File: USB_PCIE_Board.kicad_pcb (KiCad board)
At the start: 4 copper layers, 98.2 x 111.5 mm, 171 parts, among them J1 Bus_PCI_Express_x1, J2 0484050001, J3 0484050001, J4 0484050001, J5 0484050001, Q1 2SA1576AT106R, Q2 2SC4081T106R, Q4 DMT6016LSS-13, Q5 SI4134DY-T1-GE3, U1 UPD720201K8-711-BAC-A, U10 AP2191SG-13, U11 AP2191SG-13, U12 SP3011-06UTG, U13 SP3011-06UTG, U14 SP3011-06UTG, U15 SP3011-06UTG, U2 MX25L4006EM1I-12G, U3 LM22678TJ-5.0/NOPB, U4 LTC3872ETS8-TRPBF, U5 RT5762CHGH6F, U6 641737-1, U7 AP7215-33YG-13, U8 AP2191SG-13, U9 AP2191SG-13, X1 CS14522-24M

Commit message: Fix some DRC no-connect issues
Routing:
- net GND: track 86.0 -> 98.7 mm, vias 164 -> 167
- added copper zone on In2.Cu, net GND
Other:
- outline, holes or cut-outs redrawn
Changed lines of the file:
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@@
 		(layer "Edge.Cuts")
 	)
+	(gr_circle
+		(center 90.236099 106.301955)
+		(end 91.05 106.301955)
+		(stroke
+			(width 0.2)
+			(type default)
+		)
+		(fill no)
+		(layer "Edge.Cuts")
+	)
 	(gr_line
 		(start 92.79875 138.837708)
@@
 	)
 	(via
-		(at 93.9 100.8)
+		(at 93.82 100.28)
 		(size 0.35)
 		(drill 0.2)
@@
 	)
 	(via
+		(at 91.475 106.275)
+		(size 1)
+		(drill 0.4)
+		(layers "F.Cu" "B.Cu")
+		(net "GND")
+	)
+	(via
 		(at 86.4 101.2)
 		(size 0.35)
@@
 	)
 	(via
+		(at 90.225 107.525)
+		(size 1)
+		(drill 0.4)
+		(layers "F.Cu" "B.Cu")
+		(net "GND")
+	)
+	(via
 		(at 111.15 63.3)
 		(size 1)
@@
 	)
 	(via
+		(at 89 106.3)
+		(size 1)
+		(drill 0.4)
+		(layers "F.Cu" "B.Cu")
+		(net "GND")
+	)
+	(via
 		(at 124.303098 93.143309)
 		(size 0.35)
@@
 	)
 	(via
-		(at 90.2249 106.299999)
-		(size 1)
-		(drill 0.4)
+		(at 90.212351 112.228286)
+		(size 0.35)
+		(drill 0.2)
 		(layers "F.Cu" "B.Cu")
 		(net "GND")
 	)
 	(via
-		(at 90.212351 112.228286)
-		(size 0.35)
-		(drill 0.2)
+		(at 90.25 105)
+		(size 1)
+		(drill 0.4)
 		(layers "F.Cu" "B.Cu")
 		(net "GND")
@@
 	)
 	(segment
+		(start 113.6 142.3)
+		(end 113.5 142.3)
+		(width 0.5)
+		(layer "B.Cu")
+		(net "GND")
+	)
+	(segment
 		(start 84.3 102.7)
 		(end 84.3025 102.7)
@@
 	)
 	(segment
+		(start 115.7 142.3)
+		(end 115.999588 142.599588)
+		(width 0.5)
+		(layer "B.Cu")
+		(net "GND")
+	)
+	(segment
+		(start 93.81 100.29)
+		(end 93.81 100.36)
+		(width 0.2)
+		(layer "B.Cu")
+		(net "GND")
+	)
+	(segment
 		(start 93.13 112.17)
 		(end 93.13 111.53)
@@
 	)
 	(segment
+		(start 93.4225 100.7475)
+		(end 93.4225 100.8)
+		(width 0.2)
+		(layer "B.Cu")
+		(net "GND")
+	)
+	(segment
 		(start 86.4 101.2)
 		(end 87.0425 101.2)
@@
 	)
 	(segment
-		(start 93.9 100.8)
-		(end 93.4225 100.8)
-		(width 0.2)
-		(layer "B.Cu")
-		(net "GND")
-	)
-	(segment
 		(start 92.633072 100.286055)
 		(end 92.413945 100.286055)
@@
 	)
 	(segment
+		(start 113.1 142.7)
+		(end 113.1 146.3)
+		(width 0.5)
+		(layer "B.Cu")
+		(net "GND")
+	)
+	(segment
 		(start 84.9 110.2)
 		(end 84.9 109.4825)
@@
 	)
 	(segment
+		(start 115.999588 142.599588)
+		(end 115.999588 146.3)
+		(width 0.5)
+		(layer "B.Cu")
+		(net "GND")
+	)
+	(segment
 		(start 84.9 109.4825)
 		(end 85.0125 109.37)
@@
 	)
 	(segment
+		(start 113.5 142.3)
+		(end 113.1 142.7)
+		(width 0.5)
+		(layer "B.Cu")
+		(net "GND")
+	)
+	(segment
 		(start 84.39 105.39)
 		(end 84.995 105.39)
@@
 	)
 	(segment
+		(start 93.82 100.28)
+		(end 93.81 100.29)
+		(width 0.2)
+		(layer "B.Cu")
+		(net "GND")
+	)
+	(segment
 		(start 84.3 105.1)
 		(end 84.3 105.3)
@@
 	)
 	(segment
+		(start 110.148639 142.451361)
+		(end 110.148639 146.3)
+		(width 0.2)
+		(layer "B.Cu")
+		(net "GND")
+	)
+	(segment
 		(start 87.778884 112.232802)
 		(end 87.778884 111.946116)
@@
 	)
 	(segment
+		(start 110.3 142.3)
+		(end 110.148639 142.451361)
+		(width 0.2)
+		(layer "B.Cu")
+		(net "GND")
+	)
+	(segment
 		(start 91.418327 100.281673)
 		(end 91.13 100.57)
@@
 	)
 	(segment
+		(start 93.81 100.36)
+		(end 93.4225 100.7475)
+		(width 0.2)
+		(layer "B.Cu")
+		(net "GND")
+	)
+	(segment
 		(start 91.13 100.57)
 		(end 91.13 101.0925)
@@
 	)
 	(segment
-		(start 84.6 114.3)
-		(end 84.85 114.05)
+		(start 98 135.5)
+		(end 92.7 130.2)
 		(width 0.2)
 		(layer "F.Cu")
@@
 	)
 	(segment
-		(start 98 135.5)
-		(end 92.7 130.2)
+		(start 87.424901 110.975099)
+		(end 85.8 112.6)
 		(width 0.2)
 		(layer "F.Cu")
@@
 	)
 	(segment
+		(start 84.6 114.3)
+		(end 85.8 113.1)
+		(width 0.2)
+		(layer "F.Cu")
+		(net "PERSTB")
+	)
+	(segment
 		(start 92.7 130.2)
 		(end 88.1 130.2)
@@
 		(net "PERSTB")
 	)
-	(segment
-		(start 87.424901 110.975099)
-		(end 85.8 112.6)
-		(width 0.2)
-		(layer "F.Cu")
-		(net "PERSTB")
-	)
-	(segment
-		(start 85.8 113.1)
-		(end 84.6 114.3)
-		(width 0.2)
-		(layer "F.Cu")
-		(net "PERSTB")
-	)
 	(via
 		(at 98 135.5)
@@
 	)
 	(segment
-		(start 107.050694 142.450694)
-		(end 107.050694 146.3)
+		(start 100.1 135.5)
+		(end 107.050694 142.450694)
 		(width 0.2)
 		(layer "B.Cu")
@@
 	)
 	(segment
-		(start 100.1 135.5)
-		(end 107.050694 142.450694)
+		(start 107.050694 142.450694)
+		(end 107.050694 146.3)
 		(width 0.2)
 		(layer "B.Cu")
@@
 			)
 		)
+	)
+	(zone
+		(net "GND")
+		(layer "In2.Cu")
+		(hatch none 0.5)
+		(priority 65)
+		(connect_pads yes
+			(clearance 0.25)
+		)
+		(min_thickness 0.25)
+		(fill yes
+			(thermal_gap 0.5)
+			(thermal_bridge_width 0.5)
+			(island_removal_mode 0)
+		)
+		(polygon
+			(pts
+				(xy 96.6 136.4) (xy 101.2 136.4) (xy 104.2 133.4) (xy 108.6 133.4) (xy 109.6 134.4) (xy 116.8 134.4)
+				(xy 116.8 149.8) (xy 96.4 149.8)
+			)
+		)

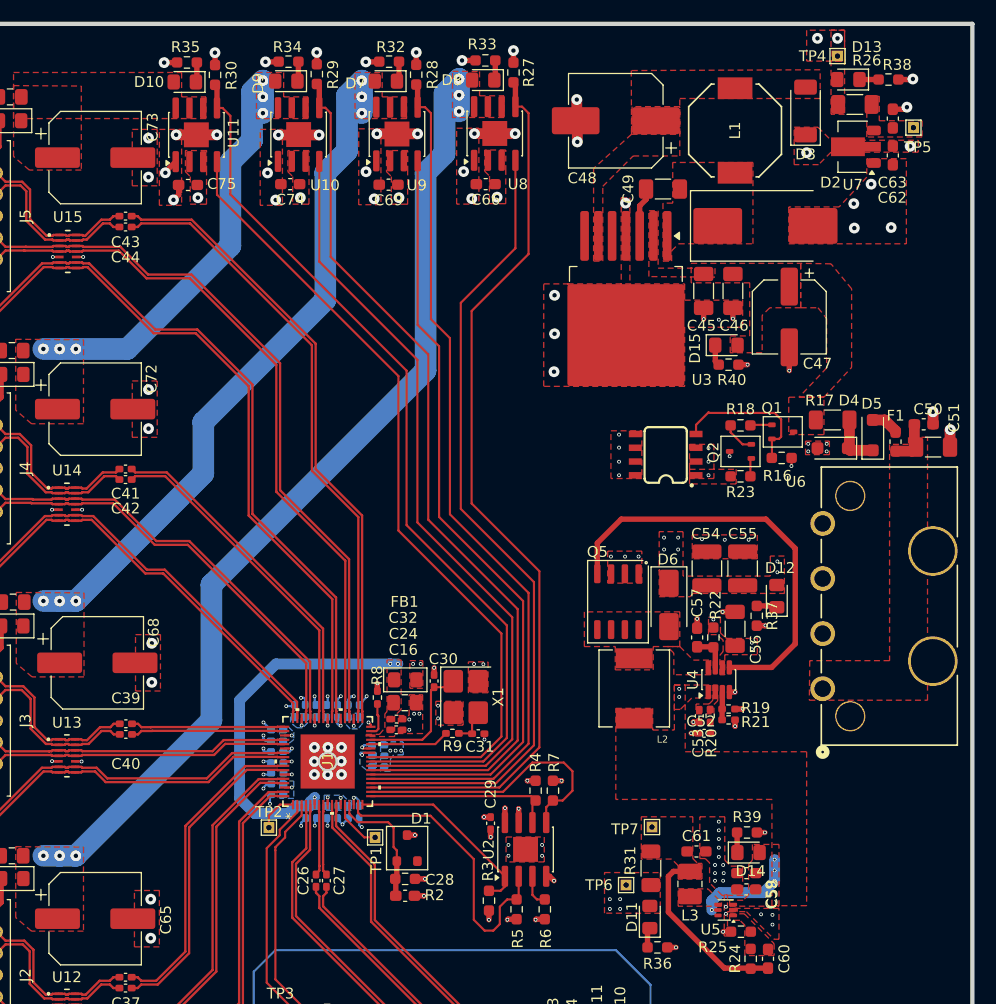
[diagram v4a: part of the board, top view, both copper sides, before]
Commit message: Replaced and rerouted host chip decoupling capacitors
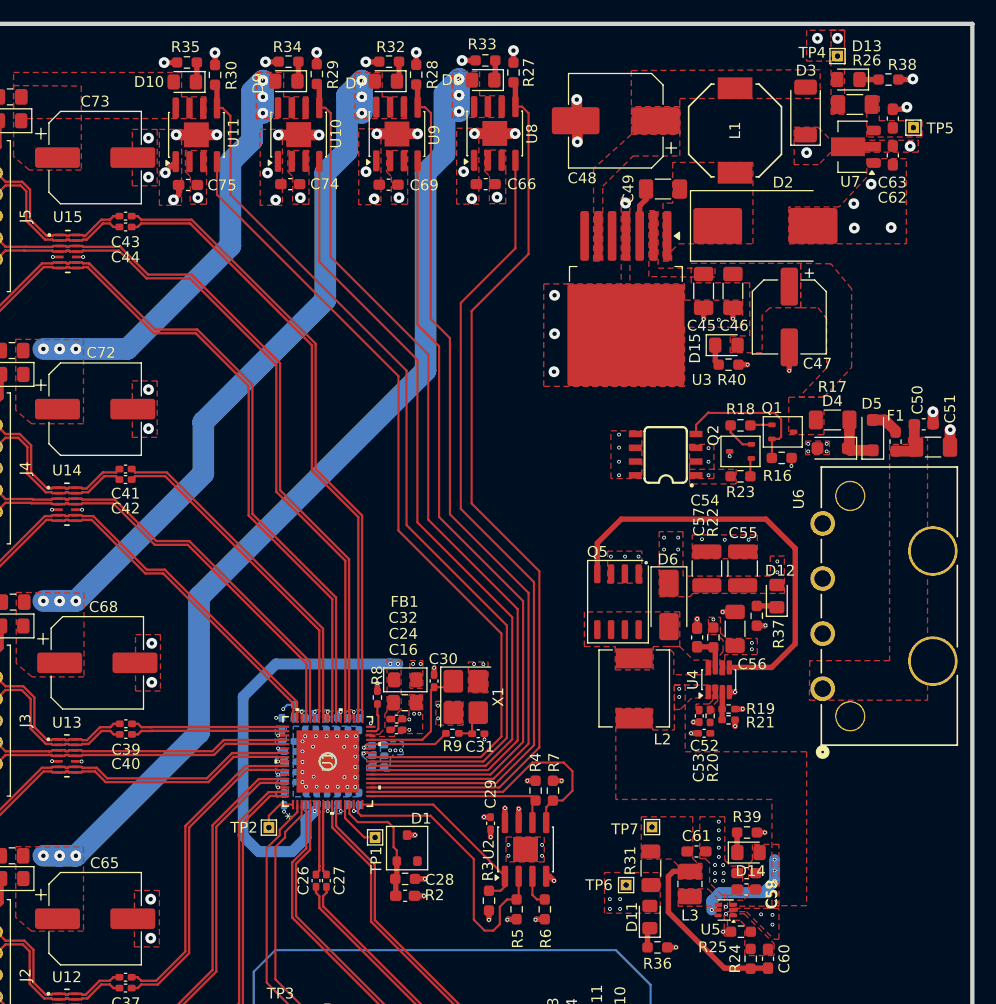
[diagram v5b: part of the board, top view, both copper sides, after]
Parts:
- moved C2 1.21 mm to (93.1, 109.7), turned to -90 degrees
- moved C4 1.21 mm to (86.8, 105.4), turned to 180 degrees
- moved C7 1.21 mm to (90.2, 109.8), turned to -90 degrees
- moved C12 1.21 mm to (91.2, 109.8), turned to -90 degrees
- moved C3 1.21 mm to (86.8, 108.2), turned to 180 degrees
- moved C8 1.21 mm to (86.8, 106.3), turned to 180 degrees
- moved C17 1.21 mm to (88.2, 109.8), turned to -90 degrees
- moved C25 1.21 mm to (89.2, 109.8), turned to 90 degrees
- moved C20 1.21 mm to (92.1, 109.8), turned to 90 degrees
- moved C6 1.21 mm to (88.2, 102.8), turned to 90 degrees
- moved C14 1.20 mm to (86.8, 107.3), turned to 180 degrees
- moved C10 1.20 mm to (89.1, 102.8), turned to 90 degrees
- moved C13 1.19 mm to (92.1, 102.8), turned to 90 degrees
- moved C23 1.19 mm to (93.1, 102.8), turned to -90 degrees
- moved C5 1.19 mm to (91.1, 102.8), turned to 90 degrees
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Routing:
- net GND: track 98.7 -> 83.0 mm, vias 167 -> 168
- net +1V05: track 9.71 -> 4.86 mm
- net +3V3A: track 36.3 -> 38.1 mm
- net +3V3_DUAL: track 21.0 -> 19.3 mm
- added copper zone on B.Cu, net +3V3A
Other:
- outline, holes or cut-outs redrawn

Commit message: Fix skew on differential pair lines and fix DRC errors from Silkscreen overlaps
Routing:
- net +3V3_INT: track 30.3 -> 33.4 mm
- net +1V05: track 4.86 -> 6.06 mm
- net U2D3P: track 49.1 -> 50.2 mm
- net U2D4P: track 68.0 -> 69.1 mm
- net +3V3A: track 38.1 -> 39.0 mm
- net +3V3_DUAL: track 19.3 -> 19.9 mm
- net PERSTB: track 50.4 -> 49.8 mm
- net U3RXD1N: track 65.9 -> 66.4 mm
- net U2D1P: track 84.4 -> 84.9 mm
- net U3RXD2N: track 40.3 -> 40.8 mm
- net U3TXD1_HN: track 57.6 -> 58.1 mm
- net U2D2P: track 57.5 -> 58.0 mm
- net U3TXD2_HN: track 31.5 -> 32.0 mm
- net GND: vias 168 -> 172

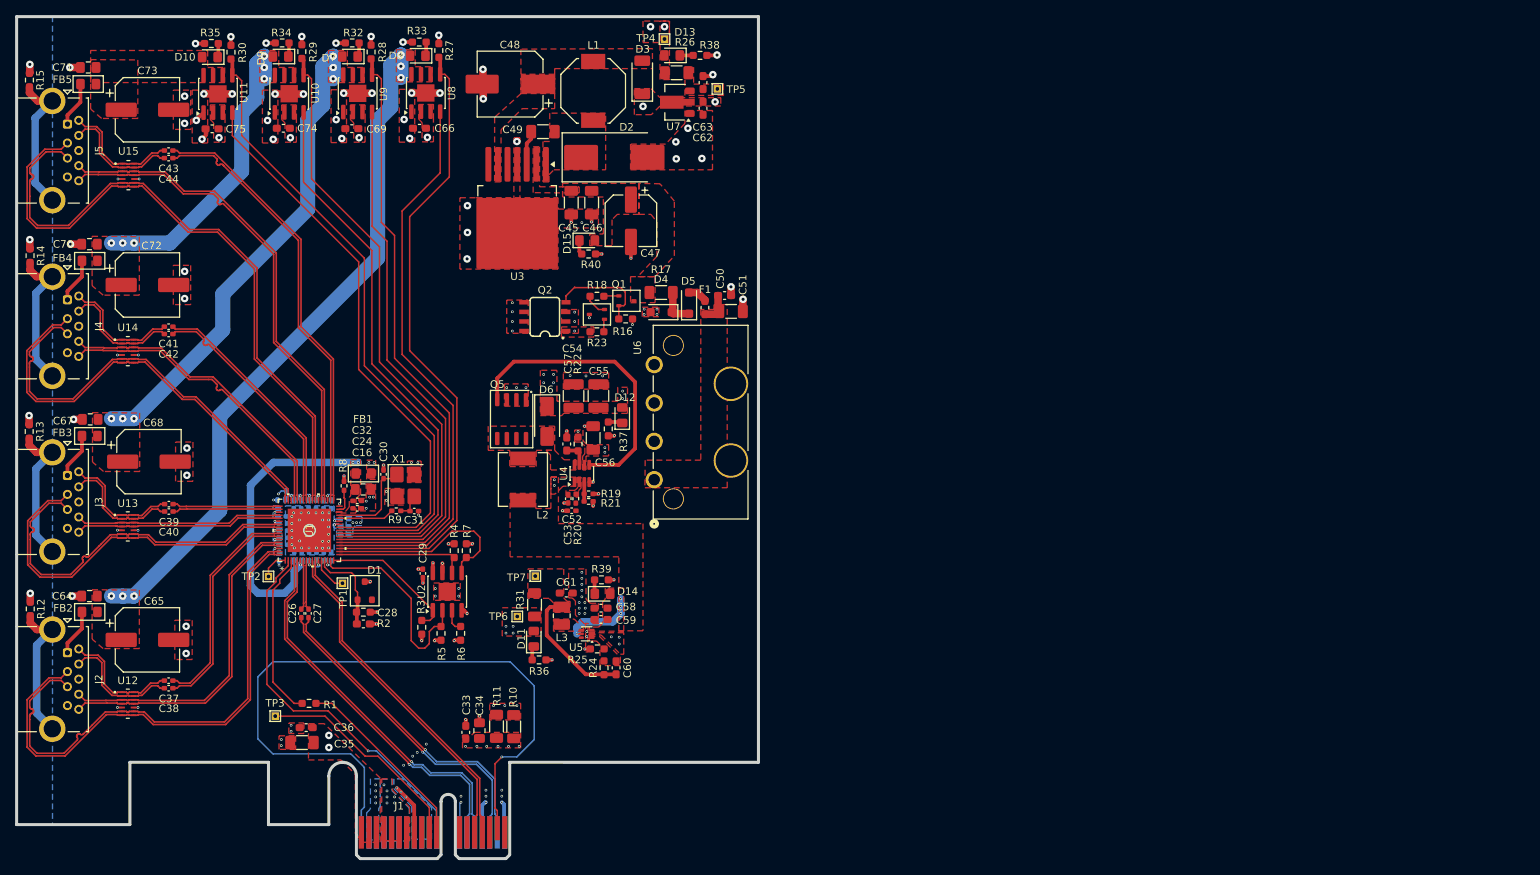
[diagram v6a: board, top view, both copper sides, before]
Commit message: Add mounting hole symbols to schematic and continue PCB DRC cleanup
Sync schematic with the board by adding H1-H4 mounting holes, and
continue working through DRC violations (dangling vias, hole
clearance, footprint mismatches) on the PCB.
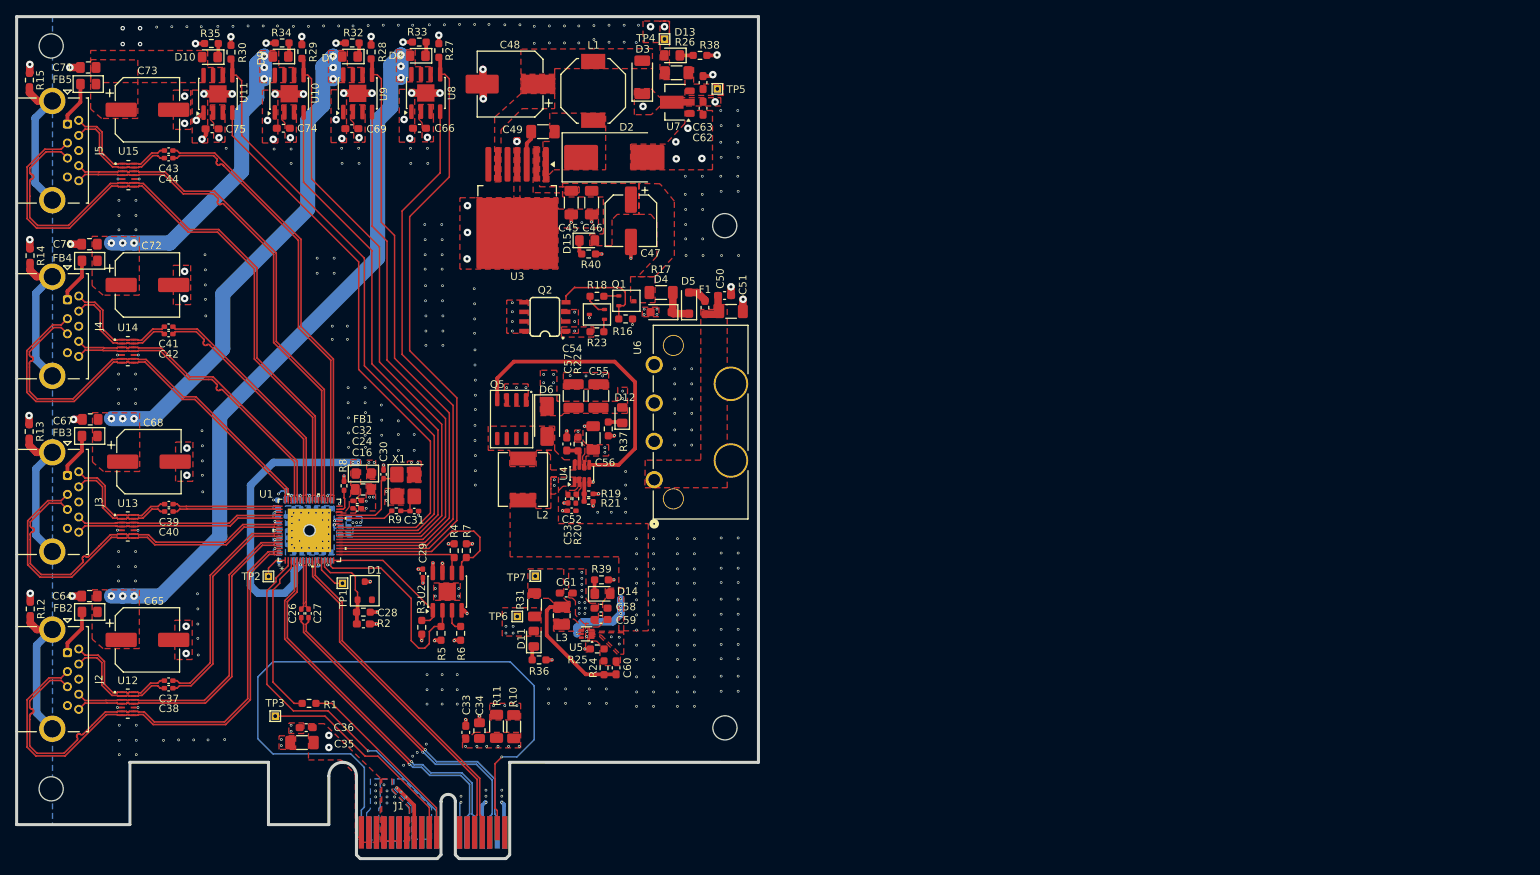
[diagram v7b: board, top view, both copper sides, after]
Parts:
- added H1: MountingHole, MountingHole:MountingHole_3.2mm_M3, F.Cu at (56.0, 42.1)
- added H2: MountingHole, MountingHole:MountingHole_3.2mm_M3, F.Cu at (56.0, 140.5)
- added H3: MountingHole, MountingHole:MountingHole_3.2mm_M3, F.Cu at (145.2, 66.0)
- added H4: MountingHole, MountingHole:MountingHole_3.2mm_M3, F.Cu at (145.2, 132.4)
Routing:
- net VCCCH4: track 92.3 -> 94.4 mm
- net VCCCH3: track 64.9 -> 66.4 mm
- net GND: vias 172 -> 461
